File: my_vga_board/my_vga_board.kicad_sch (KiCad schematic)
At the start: 25 parts, among them J4 L77HDE15SD1CH4F, SW2 SW_Push, SW3 SW_Push, SW4 SW_Push

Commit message: updated commit
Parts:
- removed R20, R21, R22: 1k, Resistor_SMD:R_0402_1005Metric, symbol Device:R
- removed SW2, SW3, SW4: SW_Push, Button_Switch_SMD:SW_Push_1P1T_NO_Vertical_Wuerth_434133025816, symbol Switch:SW_Push
- gave numbers to parts that had none: 1
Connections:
- net GPIO5: now reaches U1.7 (GPIO5)
- no-connect marks 22 -> 19
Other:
- note added: "SD_CLK"
- note removed: "Button A"
- note removed: "Button B"
- note removed: "Button C"

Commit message: adding power circuit, some layout schtuff
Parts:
- added C1: 0.33uF, Capacitor_THT:CP_Radial_D5.0mm_P2.00mm, symbol Device:C
- added C2: 0.1uF, Capacitor_THT:CP_Radial_D5.0mm_P2.00mm, symbol Device:C
- added J1: Barrel_Jack, Connector_BarrelJack:BarrelJack_Horizontal, symbol Connector:Barrel_Jack
- added U2: LM7805_TO220, Package_TO_SOT_THT:TO-220-3_Vertical, symbol Regulator_Linear:LM7805_TO220
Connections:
- net GND: now also C1.2, C2.2, J1.2, U2.2 (GND)
- net +5V: now reaches U1.39 (VSYS)
- net +5V: now also C2.1, U2.3 (VO)
- new net: C1.1, J1.1, U2.1 (VI)
- no-connect marks 19 -> 18
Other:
- note added: "12V In"
- note added: "Power"
- moved on the sheet: R10, R11, U1

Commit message: I don't know, some changes?
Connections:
- no-connect marks 18 -> 20
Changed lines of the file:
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@@
   (no_connect (at 255.27 87.63))
   (no_connect (at 240.03 102.87))
+  (no_connect (at 88.9 147.32))
   (no_connect (at 255.27 92.71))
   (no_connect (at 104.14 93.98))
@@
   (no_connect (at 240.03 100.33))
   (no_connect (at 104.14 106.68))
+  (no_connect (at 83.82 147.32))
   (wire (pts (xy 196.85 69.85) (xy 199.39 69.85))
     (stroke (width 0) (type default) (color 0 0 0 0))

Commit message: adding stubs for schematic comments section
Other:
- title: Simplified RPI-PVSA    VGA -> Simplified Pico VGA
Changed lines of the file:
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@@
   (paper "A4")
   (title_block
-    (title "Simplified RPI-PVSA    VGA")
-    (date "2022-03-17")
+    (title "Simplified Pico VGA")
+    (date "2022-12-07")
+    (comment 3 "License: MIT")
+    (comment 4 "Author: Ben Pohlman")
   )
   (junction (at 237.49 118.11) (diameter 0) (color 0 0 0 0)

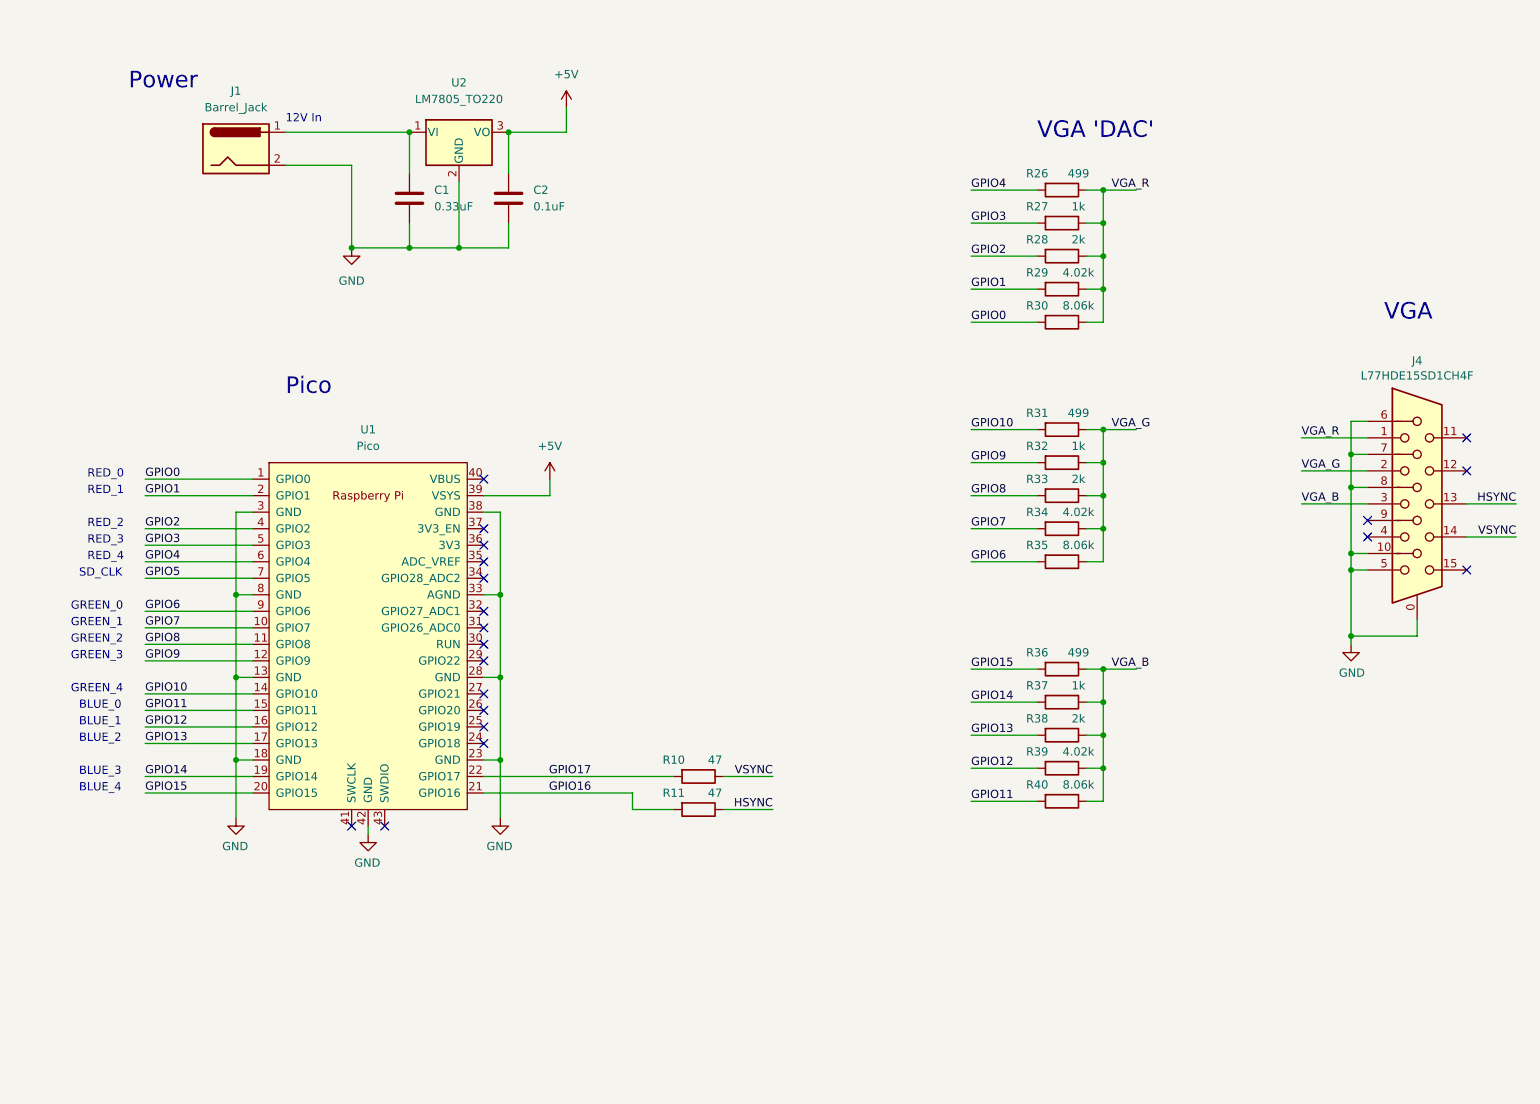
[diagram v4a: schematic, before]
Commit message: better footprints for resistance
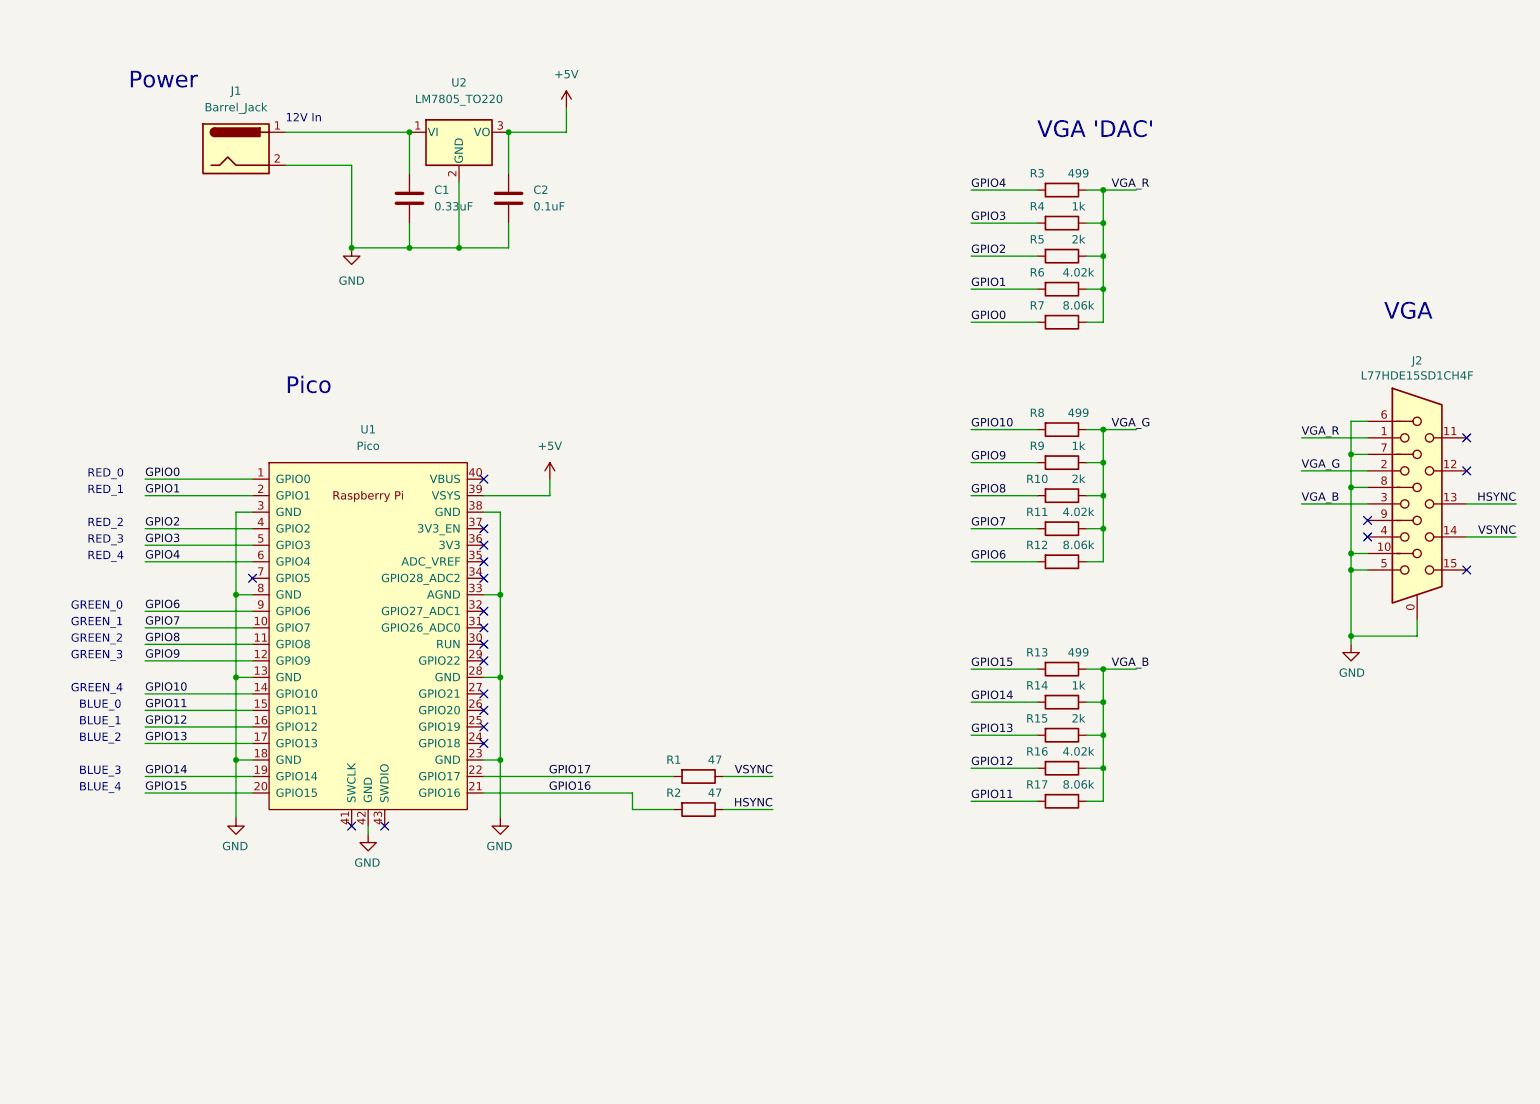
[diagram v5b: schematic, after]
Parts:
- R1: renamed from R10; footprint Resistor_SMD:R_0402_1005Metric -> Resistor_THT:R_Axial_DIN0207_L6.3mm_D2.5mm_P7.62mm_Horizontal
- R10: renamed from R33; footprint Resistor_SMD:R_0402_1005Metric -> Resistor_THT:R_Axial_DIN0207_L6.3mm_D2.5mm_P7.62mm_Horizontal
- R11: renamed from R34; footprint Resistor_SMD:R_0402_1005Metric -> Resistor_THT:R_Axial_DIN0207_L6.3mm_D2.5mm_P7.62mm_Horizontal
- R12: renamed from R35; footprint Resistor_SMD:R_0402_1005Metric -> Resistor_THT:R_Axial_DIN0207_L6.3mm_D2.5mm_P7.62mm_Horizontal
- R13: renamed from R36; footprint Resistor_SMD:R_0402_1005Metric -> Resistor_THT:R_Axial_DIN0207_L6.3mm_D2.5mm_P7.62mm_Horizontal
- R14: renamed from R37; footprint Resistor_SMD:R_0402_1005Metric -> Resistor_THT:R_Axial_DIN0207_L6.3mm_D2.5mm_P7.62mm_Horizontal
- R15: renamed from R38; footprint Resistor_SMD:R_0402_1005Metric -> Resistor_THT:R_Axial_DIN0207_L6.3mm_D2.5mm_P7.62mm_Horizontal
- R16: renamed from R39; footprint Resistor_SMD:R_0402_1005Metric -> Resistor_THT:R_Axial_DIN0207_L6.3mm_D2.5mm_P7.62mm_Horizontal
- R17: renamed from R40; footprint Resistor_SMD:R_0402_1005Metric -> Resistor_THT:R_Axial_DIN0207_L6.3mm_D2.5mm_P7.62mm_Horizontal
- R2: renamed from R11; footprint Resistor_SMD:R_0402_1005Metric -> Resistor_THT:R_Axial_DIN0207_L6.3mm_D2.5mm_P7.62mm_Horizontal
- R3: renamed from R26; footprint Resistor_SMD:R_0402_1005Metric -> Resistor_THT:R_Axial_DIN0207_L6.3mm_D2.5mm_P7.62mm_Horizontal
- R4: renamed from R27; footprint Resistor_SMD:R_0402_1005Metric -> Resistor_THT:R_Axial_DIN0207_L6.3mm_D2.5mm_P7.62mm_Horizontal
- R5: renamed from R28; footprint Resistor_SMD:R_0402_1005Metric -> Resistor_THT:R_Axial_DIN0207_L6.3mm_D2.5mm_P7.62mm_Horizontal
- R6: renamed from R29; footprint Resistor_SMD:R_0402_1005Metric -> Resistor_THT:R_Axial_DIN0207_L6.3mm_D2.5mm_P7.62mm_Horizontal
- R7: renamed from R30; footprint Resistor_SMD:R_0402_1005Metric -> Resistor_THT:R_Axial_DIN0207_L6.3mm_D2.5mm_P7.62mm_Horizontal
- R8: renamed from R31; footprint Resistor_SMD:R_0402_1005Metric -> Resistor_THT:R_Axial_DIN0207_L6.3mm_D2.5mm_P7.62mm_Horizontal
- R9: renamed from R32; footprint Resistor_SMD:R_0402_1005Metric -> Resistor_THT:R_Axial_DIN0207_L6.3mm_D2.5mm_P7.62mm_Horizontal
- renumbered J4 to J2
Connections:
- net GPIO5: no longer names the net of U1.7 (GPIO5)
- no-connect marks 20 -> 21
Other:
- note removed: "SD_CLK"

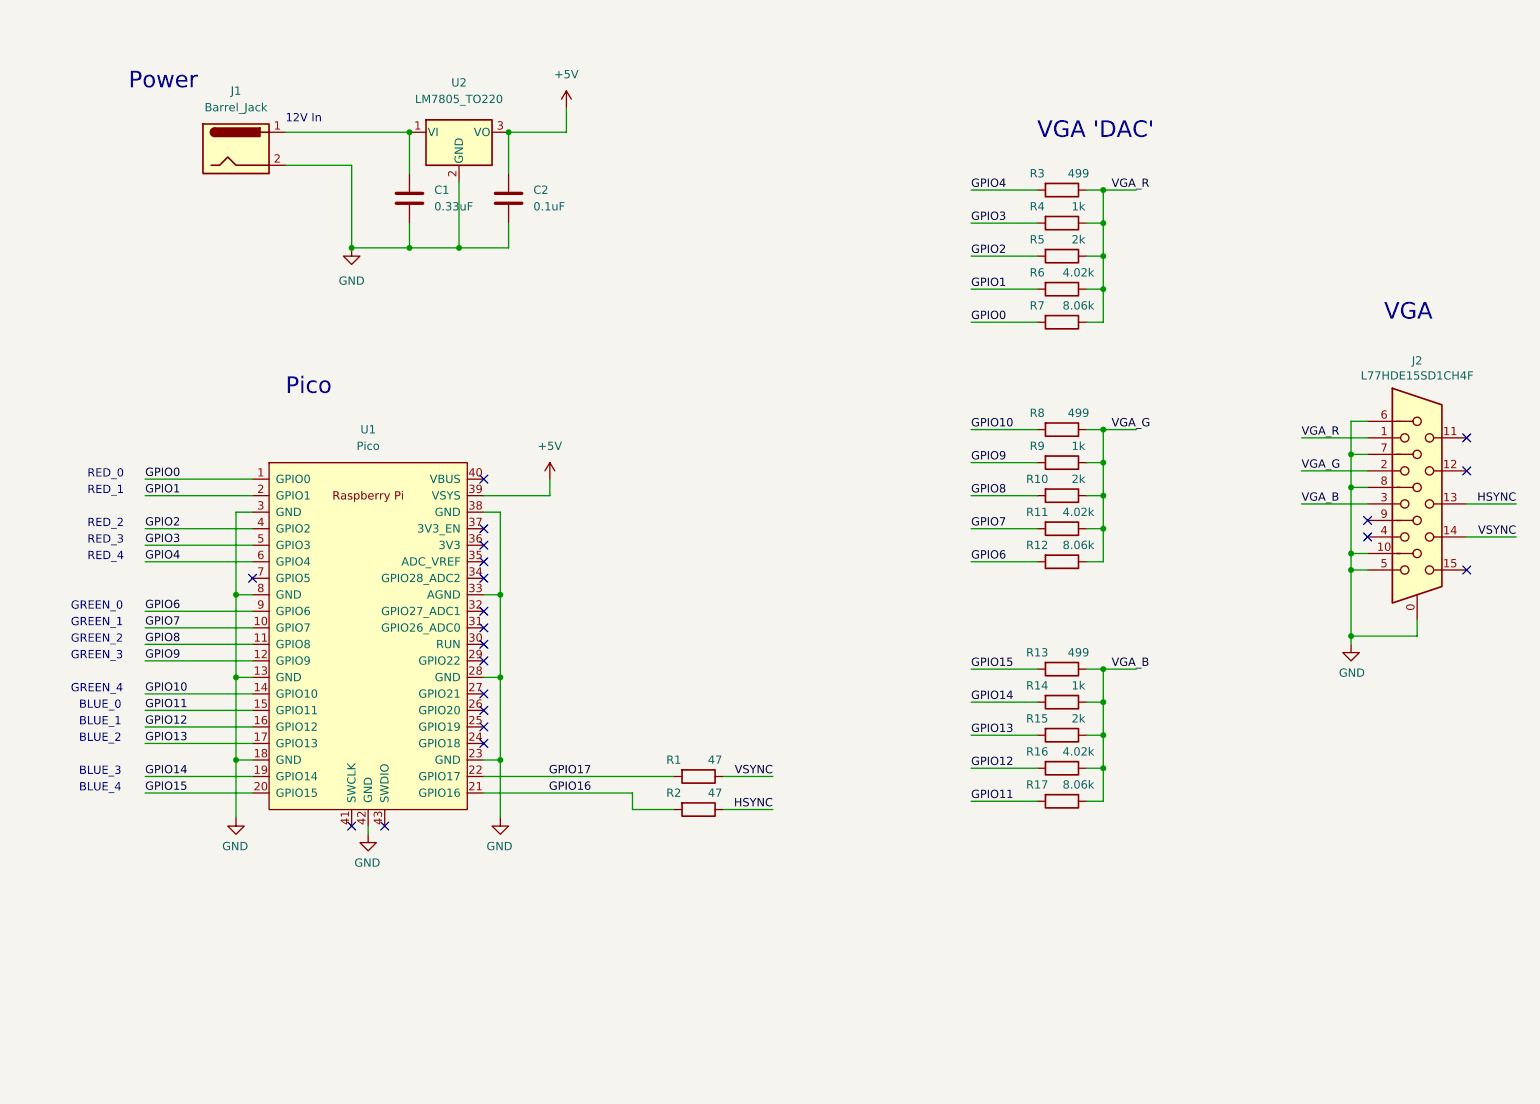
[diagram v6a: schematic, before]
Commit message: now supports multiplayer... over I2C?
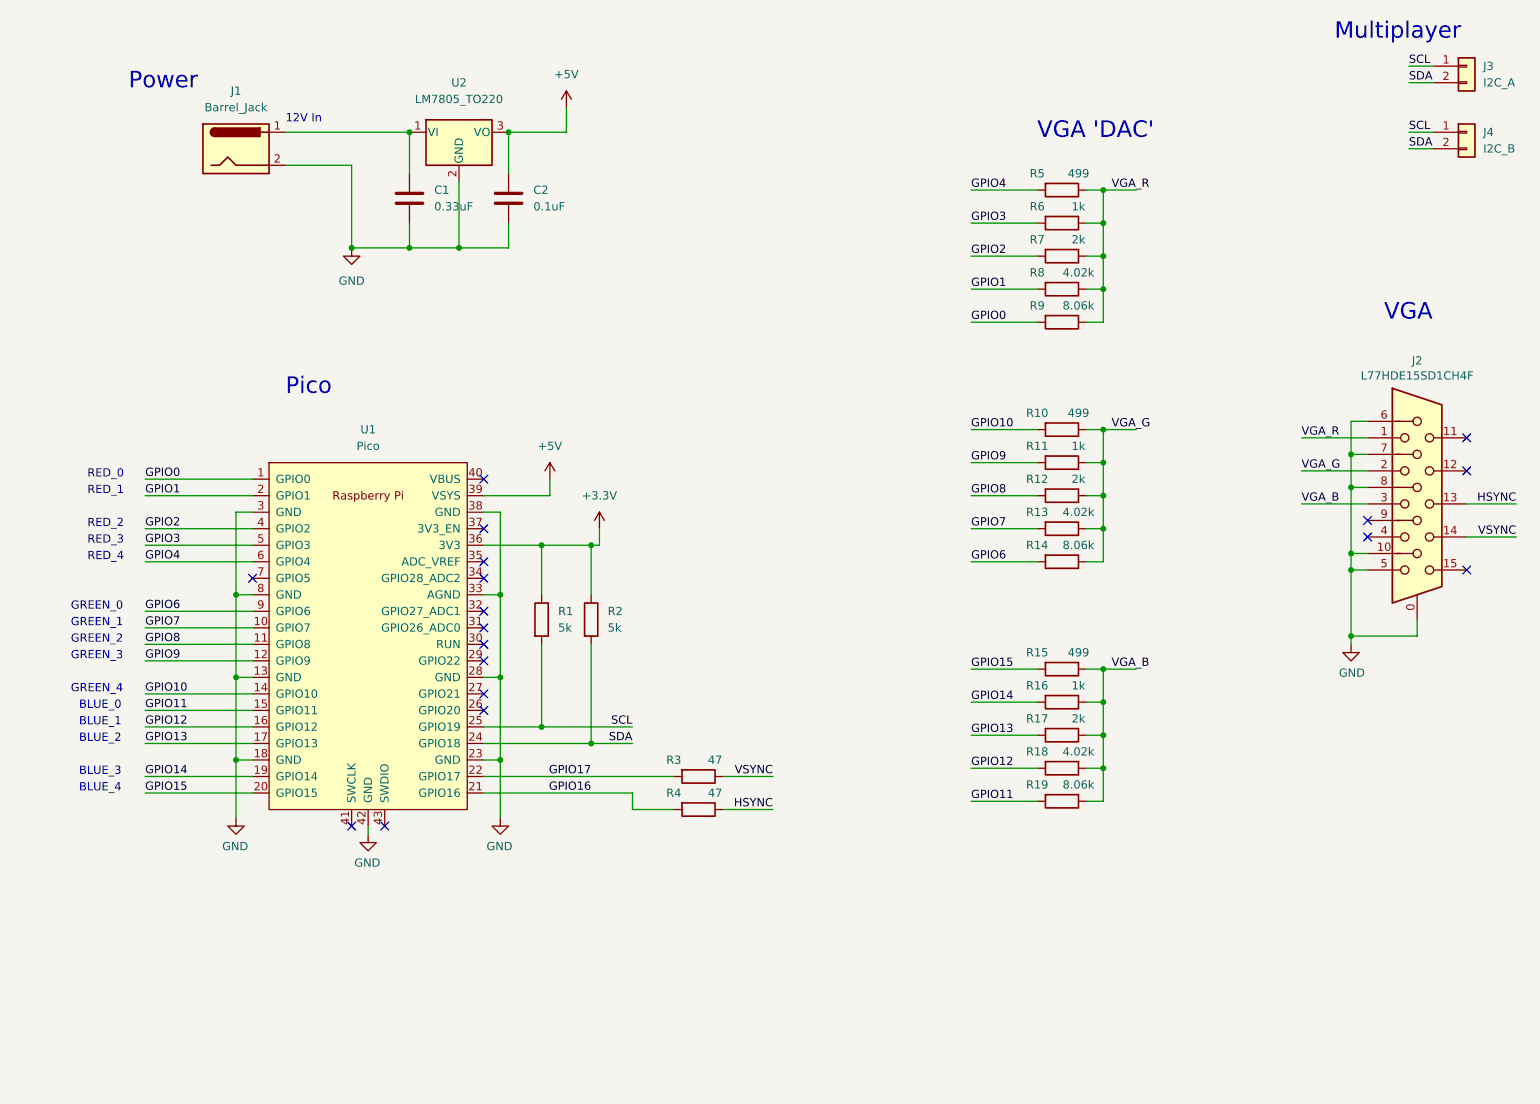
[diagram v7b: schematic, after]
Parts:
- added J3: I2C_A, Connector_PinHeader_2.54mm:PinHeader_1x02_P2.54mm_Horizontal, symbol Connector_Generic:Conn_01x02
- added J4: I2C_B, Connector_PinHeader_2.54mm:PinHeader_1x02_P2.54mm_Horizontal, symbol Connector_Generic:Conn_01x02
- added R1, R2: 5k, Resistor_THT:R_Axial_DIN0207_L6.3mm_D2.5mm_P7.62mm_Horizontal, symbol Device:R
- renumbered R8 to R10, R9 to R11, R10 to R12, R11 to R13, R12 to R14, R13 to R15, R14 to R16, R15 to R17, R16 to R18, R17 to R19, R1 to R3, R2 to R4, R3 to R5, R4 to R6, R5 to R7, R6 to R8, R7 to R9
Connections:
- net SDA: now reaches U1.24 (GPIO18)
- net SDA: now also J3.2 (Pin_2), J4.2 (Pin_2), R2.2
- net SCL: now reaches U1.25 (GPIO19)
- net SCL: now also J3.1 (Pin_1), J4.1 (Pin_1), R1.2
- net +3.3V: now reaches U1.36 (3V3)
- net +3.3V: now also R1.1, R2.1
- no-connect marks 21 -> 18
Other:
- note added: "Multiplayer"

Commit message: now with mounting holes, and accredidation, ooooh
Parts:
- added H1, H2, H3: MountingHole, MountingHole:MountingHole_4.3mm_M4, symbol Mechanical:MountingHole
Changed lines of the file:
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@@
     (pin "1")
+  )
+  (symbol (lib_id "Mechanical:MountingHole") (at 95.25 175.26 0) (unit 1)
+    (in_bom yes) (on_board yes) (fields_autoplaced)
+    (property "Reference" "H1" (id 0) (at 97.79 173.9899 0)
+      (effects (font (size 1.27 1.27)) (justify left))
+    )
+    (property "Value" "MountingHole" (id 1) (at 97.79 176.5299 0)
+      (effects (font (size 1.27 1.27)) (justify left))
+    )
+    (property "Footprint" "MountingHole:MountingHole_4.3mm_M4" (id 2) (at 95.25 175.26 0)
+      (effects (font (size 1.27 1.27)) hide)
+    )
+    (property "Datasheet" "~" (id 3) (at 95.25 175.26 0)
+      (effects (font (size 1.27 1.27)) hide)
+    )
   )
   (symbol (lib_id "Device:C") (at 107.95 50.8 0) (unit 1)
@@
     (pin "1")
     (pin "2")
+  )
+  (symbol (lib_id "Mechanical:MountingHole") (at 95.25 185.42 0) (unit 1)
+    (in_bom yes) (on_board yes) (fields_autoplaced)
+    (property "Reference" "H3" (id 0) (at 97.79 184.1499 0)
+      (effects (font (size 1.27 1.27)) (justify left))
+    )
+    (property "Value" "MountingHole" (id 1) (at 97.79 186.6899 0)
+      (effects (font (size 1.27 1.27)) (justify left))
+    )
+    (property "Footprint" "MountingHole:MountingHole_4.3mm_M4" (id 2) (at 95.25 185.42 0)
+      (effects (font (size 1.27 1.27)) hide)
+    )
+    (property "Datasheet" "~" (id 3) (at 95.25 185.42 0)
+      (effects (font (size 1.27 1.27)) hide)
+    )
+  )
+  (symbol (lib_id "Mechanical:MountingHole") (at 95.25 180.34 0) (unit 1)
+    (in_bom yes) (on_board yes) (fields_autoplaced)
+    (property "Reference" "H2" (id 0) (at 97.79 179.0699 0)
+      (effects (font (size 1.27 1.27)) (justify left))
+    )
+    (property "Value" "MountingHole" (id 1) (at 97.79 181.6099 0)
+      (effects (font (size 1.27 1.27)) (justify left))
+    )
+    (property "Footprint" "MountingHole:MountingHole_4.3mm_M4" (id 2) (at 95.25 180.34 0)
+      (effects (font (size 1.27 1.27)) hide)
+    )
+    (property "Datasheet" "~" (id 3) (at 95.25 180.34 0)
+      (effects (font (size 1.27 1.27)) hide)
+    )
   )
   (symbol (lib_id "power:+5V") (at 114.3 93.98 0) (unit 1)
@@
       (reference "C2") (unit 1) (value "0.1uF") (footprint "Capacitor_THT:CP_Radial_D5.0mm_P2.00mm")
     )
+    (path "/5960e89b-0ec9-4078-b3d2-a7827bbb94ae"
+      (reference "H1") (unit 1) (value "MountingHole") (footprint "MountingHole:MountingHole_4.3mm_M4")
+    )
+    (path "/62c44338-3ab0-4154-9ba5-7d565cb73c34"
+      (reference "H2") (unit 1) (value "MountingHole") (footprint "MountingHole:MountingHole_4.3mm_M4")
+    )
+    (path "/61630745-207c-4525-ba0c-de772b8cf63d"
+      (reference "H3") (unit 1) (value "MountingHole") (footprint "MountingHole:MountingHole_4.3mm_M4")
+    )
     (path "/0a6822c7-7adc-4e2f-ae37-35493f0a0f91"
